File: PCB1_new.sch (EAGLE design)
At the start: 73 parts

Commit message: Finished changing dimensions for PCB3 and switched out resistors for smaller ones.
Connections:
- removed net N$100: U$31.P$1
- removed net N$101: U$30.P$1
- removed net N$102: U$29.P$1
- removed net N$103: U$28.P$1
- removed net N$104: U$27.P$1
- removed net N$105: U$26.P$1
- removed net N$106: U$25.P$1
- removed net N$107: U$24.P$1
- removed net N$108: U$23.P$1
- removed net N$109: U$22.P$1
- removed net N$110: U$21.P$1
- removed net N$111: U$20.P$1
- removed net N$112: U$19.P$1
- removed net N$113: U$18.P$1
- removed net N$114: U$17.P$1
- removed net N$115: U$16.P$1
- removed net N$13: U$35.P$1
- removed net N$14: U$1.SCLR, U$3.SCLR, U$4.SCLR, U$5.SCLR
- removed net N$17: U$35.P$2
- removed net N$18: U$34.P$1
- removed net N$31: U$34.P$2
- removed net N$32: U$33.P$2
- removed net N$33: U$33.P$1
- removed net N$34: U$6.P$1
- removed net N$42: U$7.P$1
- removed net N$45: U$8.P$1
- removed net N$48: U$1.SCK, U$3.SCK, U$4.SCK, U$5.SCK
- removed net N$50: U$9.P$1
- removed net N$51: U$1.RCK, U$3.RCK, U$4.RCK, U$5.RCK
- removed net N$52: U$6.P$2
- removed net N$53: U$7.P$2
- removed net N$54: U$8.P$2
- removed net N$55: U$9.P$2
- removed net N$56: U$10.P$1
- removed net N$57: U$11.P$1
- removed net N$58: U$10.P$2
- removed net N$59: U$11.P$2
- removed net N$65: U$12.P$2
- removed net N$73: U$12.P$1
- removed net N$74: U$13.P$1
- removed net N$75: U$13.P$2
- removed net N$76: U$14.P$2
- removed net N$77: U$14.P$1
- removed net N$78: U$15.P$1
- removed net N$79: U$15.P$2
- removed net N$80: U$16.P$2
- removed net N$81: U$17.P$2
- removed net N$82: U$18.P$2
- removed net N$83: U$19.P$2
- removed net N$84: U$20.P$2
- removed net N$85: U$21.P$2
- removed net N$86: U$22.P$2
- removed net N$87: U$23.P$2
- removed net N$88: U$24.P$2
- removed net N$89: U$25.P$2
- removed net N$90: U$26.P$2
- removed net N$91: U$27.P$2
- removed net N$92: U$28.P$2
- removed net N$93: U$29.P$2
- removed net N$94: U$30.P$2
- removed net N$95: U$31.P$2
- removed net N$96: U$32.P$2
- removed net N$97: U$36.P$2
- removed net N$98: U$36.P$1
- removed net N$99: U$32.P$1
- new net RCK: U$1.RCK, U$3.RCK, U$31.P$1, U$31.P$2, U$4.RCK, U$5.RCK
- new net SCK: U$1.SCK, U$3.SCK, U$32.P$1, U$32.P$2, U$4.SCK, U$5.SCK
- new net SCLR: U$1.SCLR, U$3.SCLR, U$36.P$1, U$36.P$2, U$4.SCLR, U$5.SCLR
- net EAN: now also U$26.P$1, U$26.P$2
- net FRET1: now also U$19.P$1, U$19.P$2
- net FRET2: now also U$20.P$1, U$20.P$2
- net G: now also U$30.P$1, U$30.P$2
- net LED_SER1: now also U$15.P$1, U$15.P$2
- net LED_SER2: now also U$16.P$1, U$16.P$2
- net LED_SER3: now also U$17.P$1, U$17.P$2
- net LED_SER4: now also U$18.P$1, U$18.P$2
- net P0_0: now also U$23.P$1, U$23.P$2
- net P0_4: now also U$13.P$1, U$13.P$2
- net P0_5: now also U$22.P$1, U$22.P$2
- net P1_2: now also U$29.P$1, U$29.P$2
- net P1_3: now also U$28.P$1, U$28.P$2
- net P1_5: now also U$14.P$1, U$14.P$2
- net P1_7: now also U$21.P$1, U$21.P$2
- net P2_0: now also U$24.P$1, U$24.P$2
- net P2_4: now also U$25.P$1, U$25.P$2
- net P3_1: now also U$33.P$1, U$33.P$2
- net P3_2: now also U$6.P$1, U$6.P$2
- net P3_3: now also U$7.P$1, U$7.P$2
- net P3_4: now also U$8.P$1, U$8.P$2
- net P3_6: now also U$9.P$1, U$9.P$2
- net P3_7: now also U$10.P$1, U$10.P$2
- net RST_N: now also U$27.P$1, U$27.P$2
- net RXD: now also U$35.P$1, U$35.P$2
- net SW_BTN: now also U$12.P$1, U$12.P$2
- net TXD: now also U$34.P$1, U$34.P$2
- net WAKEUP: now also U$11.P$1, U$11.P$2

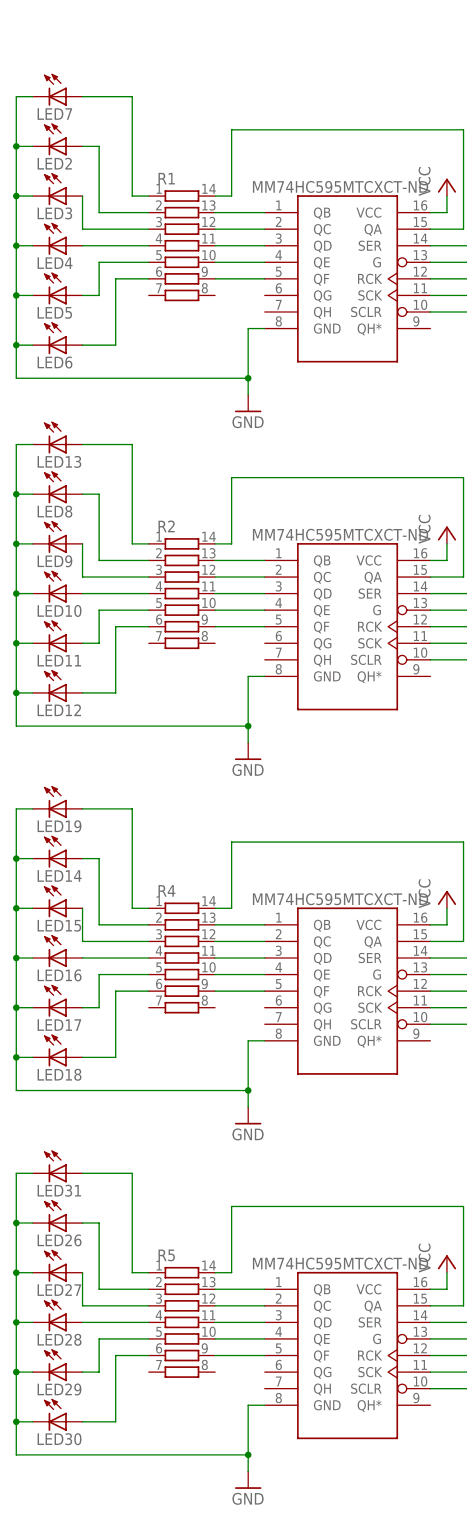
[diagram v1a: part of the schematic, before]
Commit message: Finished changes to PCB1 by switching out resistor packages and reordering the pin connections for PCB2
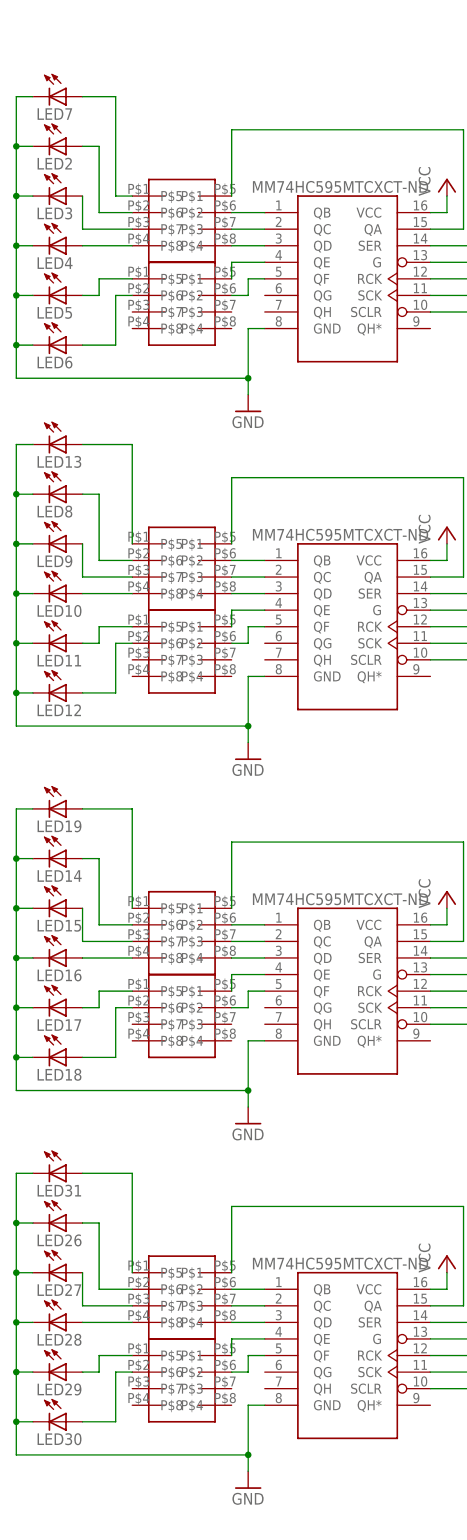
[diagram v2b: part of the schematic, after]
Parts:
- removed R1, R2, R4, R5: (no value), resistor-bourns:4814P-T01
- added U$37, U$38, U$39, U$40, U$41, U$42, U$43, U$44: MNR04MRAPJ680, ECE477_Guitutar:MNR04MRAPJ680
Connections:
- removed net N$20: R2.12, U$1.QC
- removed net N$28: LED10.A, R2.4
- removed net N$46: LED16.A, R4.4
- removed net N$70: LED28.A, R5.4
- new net N$13: U$1.QB, U$39.P$6
- new net N$14: U$1.QC, U$39.P$7
- new net N$17: LED10.A, U$39.P$4
- new net N$18: LED16.A, U$41.P$4
- net N$1: now also U$37.P$6; no longer R1.13
- net N$10: now also U$37.P$4; no longer R1.4
- net N$11: now also U$38.P$1; no longer R1.5
- net N$12: now also U$38.P$2; no longer R1.6
- net N$19: now also LED28.A, U$43.P$4; no longer R2.13, U$1.QB
- net N$2: now also U$37.P$7; no longer R1.12
- net N$21: now also U$39.P$8; no longer R2.11
- net N$22: now also U$40.P$5; no longer R2.10
- net N$23: now also U$40.P$6; no longer R2.9
- net N$24: now also U$39.P$5; no longer R2.14
- net N$25: now also U$39.P$1; no longer R2.1
- net N$26: now also U$39.P$2; no longer R2.2
- net N$27: now also U$39.P$3; no longer R2.3
- net N$29: now also U$40.P$1; no longer R2.5
- net N$3: now also U$37.P$8; no longer R1.11
- net N$30: now also U$40.P$2; no longer R2.6
- net N$35: now also U$41.P$6; no longer R4.13
- net N$36: now also U$41.P$7; no longer R4.12
- net N$37: now also U$41.P$8; no longer R4.11
- net N$38: now also U$42.P$5; no longer R4.10
- net N$39: now also U$42.P$6; no longer R4.9
- net N$4: now also U$38.P$5; no longer R1.10
- net N$40: now also U$41.P$5; no longer R4.14
- net N$41: now also U$41.P$1; no longer R4.1
- net N$43: now also U$41.P$2; no longer R4.2
- net N$44: now also U$41.P$3; no longer R4.3
- net N$47: now also U$42.P$1; no longer R4.5
- net N$49: now also U$42.P$2; no longer R4.6
- net N$5: now also U$38.P$6; no longer R1.9
- net N$6: now also U$37.P$1; no longer R1.1
- net N$60: now also U$43.P$6; no longer R5.13
- net N$61: now also U$43.P$7; no longer R5.12
- net N$62: now also U$43.P$8; no longer R5.11
- net N$63: now also U$44.P$5; no longer R5.10
- net N$64: now also U$44.P$6; no longer R5.9
- net N$66: now also U$43.P$5; no longer R5.14
- net N$67: now also U$43.P$1; no longer R5.1
- net N$68: now also U$43.P$2; no longer R5.2
- net N$69: now also U$43.P$3; no longer R5.3
- net N$7: now also U$37.P$5; no longer R1.14
- net N$71: now also U$44.P$1; no longer R5.5
- net N$72: now also U$44.P$2; no longer R5.6
- net N$8: now also U$37.P$2; no longer R1.2
- net N$9: now also U$37.P$3; no longer R1.3
